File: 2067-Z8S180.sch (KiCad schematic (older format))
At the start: 13 parts, among them J1 Conn_02x12_Odd_Even, J2 Conn_02x30_Odd_Even, U1 Z8S18020FSG, U2 IS61WV10248EDBLL-10TLI

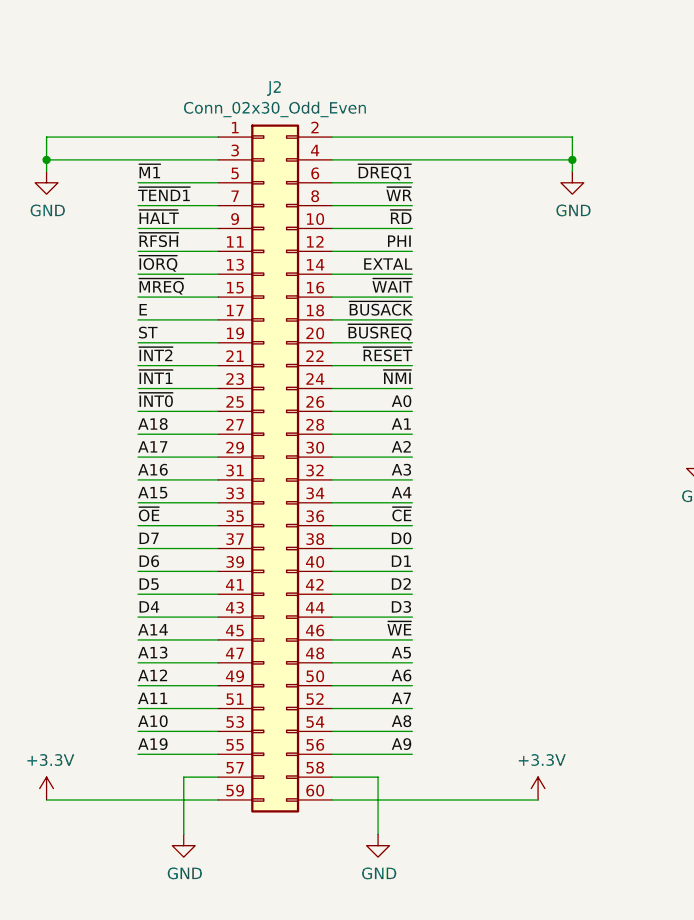
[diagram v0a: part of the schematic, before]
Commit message: Add FPGA pin number reference
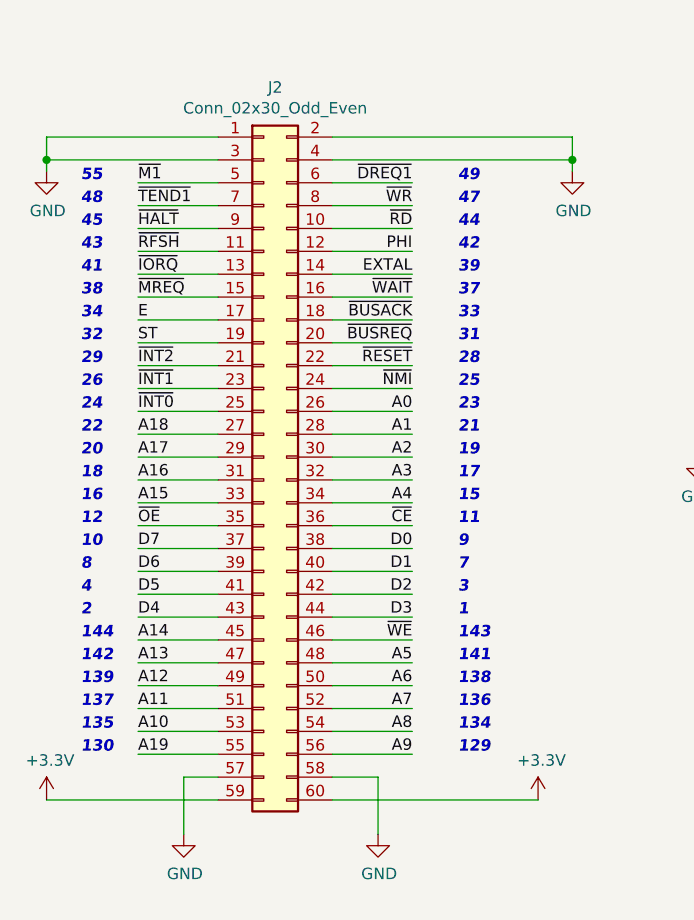
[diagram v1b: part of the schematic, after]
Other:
- note added: "1"
- note added: "10"
- note added: "11"
- note added: "12"
- note added: "129"
- note added: "130"
- note added: "134"
- note added: "135"
- note added: "136"
- note added: "137"
- note added: "138"
- note added: "139"
- note added: "141"
- note added: "142"
- note added: "143"
- note added: "144"
- note added: "15"
- note added: "16"
- note added: "17"
- note added: "18"
- note added: "19"
- note added: "2"
- note added: "20"
- note added: "21"
- note added: "22"
- note added: "23"
- note added: "24"
- note added: "25"
- note added: "26"
- note added: "28"
- note added: "29"
- note added: "3"
- note added: "31"
- note added: "32"
- note added: "33"
- note added: "34"
- note added: "37"
- note added: "38"
- note added: "39"
- note added: "4"
- note added: "41"
- note added: "42"
- note added: "43"
- note added: "44"
- note added: "45"
- note added: "47"
- note added: "48"
- note added: "49"
- note added: "55"
- note added: "7"
- note added: "8"
- note added: "9"
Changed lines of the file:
@@
 	1    0    0    -1
 $EndComp
+Text Notes 4500 3800 0    50   Italic 10
+55
+Text Notes 4500 3900 0    50   Italic 10
+48
+Text Notes 4500 4000 0    50   Italic 10
+45
+Text Notes 4500 4100 0    50   Italic 10
+43
+Text Notes 4500 4200 0    50   Italic 10
+41
+Text Notes 4500 4300 0    50   Italic 10
+38
+Text Notes 4500 4400 0    50   Italic 10
+34
+Text Notes 4500 4500 0    50   Italic 10
+32
+Text Notes 4500 4600 0    50   Italic 10
+29
+Text Notes 4500 4700 0    50   Italic 10
+26
+Text Notes 4500 4800 0    50   Italic 10
+24
+Text Notes 4500 4900 0    50   Italic 10
+22
+Text Notes 4500 5000 0    50   Italic 10
+20
+Text Notes 4500 5100 0    50   Italic 10
+18
+Text Notes 4500 5200 0    50   Italic 10
+16
+Text Notes 4500 5300 0    50   Italic 10
+12
+Text Notes 4500 5400 0    50   Italic 10
+10
+Text Notes 4500 5500 0    50   Italic 10
+8
+Text Notes 4500 5600 0    50   Italic 10
+4
+Text Notes 4500 5700 0    50   Italic 10
+2
+Text Notes 4500 5800 0    50   Italic 10
+144
+Text Notes 4500 5900 0    50   Italic 10
+142
+Text Notes 4500 6000 0    50   Italic 10
+139
+Text Notes 4500 6100 0    50   Italic 10
+137
+Text Notes 4500 6200 0    50   Italic 10
+135
+Text Notes 4500 6300 0    50   Italic 10
+130
+Text Notes 6150 6300 0    50   Italic 10
+129
+Text Notes 6150 6200 0    50   Italic 10
+134
+Text Notes 6150 6100 0    50   Italic 10
+136
+Text Notes 6150 6000 0    50   Italic 10
+138
+Text Notes 6150 5900 0    50   Italic 10
+141
+Text Notes 6150 5800 0    50   Italic 10
+143
+Text Notes 6150 5700 0    50   Italic 10
+1
+Text Notes 6150 5600 0    50   Italic 10
+3
+Text Notes 6150 5500 0    50   Italic 10
+7
+Text Notes 6150 5400 0    50   Italic 10
+9
+Text Notes 6150 5300 0    50   Italic 10
+11
+Text Notes 6150 5200 0    50   Italic 10
+15
+Text Notes 6150 5100 0    50   Italic 10
+17
+Text Notes 6150 5000 0    50   Italic 10
+19
+Text Notes 6150 4900 0    50   Italic 10
+21
+Text Notes 6150 4800 0    50   Italic 10
+23
+Text Notes 6150 4700 0    50   Italic 10
+25
+Text Notes 6150 4600 0    50   Italic 10
+28
+Text Notes 6150 4500 0    50   Italic 10
+31
+Text Notes 6150 4400 0    50   Italic 10
+33
+Text Notes 6150 4300 0    50   Italic 10
+37
+Text Notes 6150 4200 0    50   Italic 10
+39
+Text Notes 6150 4100 0    50   Italic 10
+42
+Text Notes 6150 4000 0    50   Italic 10
+44
+Text Notes 6150 3900 0    50   Italic 10
+47
+Text Notes 6150 3800 0    50   Italic 10
+49
 $EndSCHEMATC

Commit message: Thermal relief, SRAM A20
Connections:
- net GND: now also U2.42 (A20)
- no-connect marks 8 -> 7
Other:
- note added: "Copyright (C) 2019, 2023 John Winans\n\nThis documentation describes Open Hardware and is licensed under the CERN OHL v. 1.2.\n\nYou may redistribute and modify this documentation under the terms of the CERN OHL v.1.2. (http://ohwr.org/cernohl). \nThis documentation is distributed WITHOUT ANY EXPRESS OR IMPLIED WARRANTY, INCLUDING OF MERCHANTABILITY, \nSATISFACTORY QUALITY AND FITNESS FOR A PARTI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"
- note added: "IS61WV5128FBLL-10TLI\nIS61WV10248EDBLL-10TLI\nIS61WV20488BLL-10TLI"
- note added: "Viable SRAM substitutes:"
- note added: "https://github.com/johnwinans/2067-Z8S180"
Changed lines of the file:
@@
 Sheet 1 1
 Title "Z8S180 Breakout"
-Date "2023-12-10"
-Rev "1.1"
+Date "2024-02-19"
+Rev "1.2"
 Comp ""
 Comment1 ""
@@
 Text Label 12500 5900 0    50   ~ 0
 A19
-NoConn ~ 12950 6000
 Text Label 12500 6150 0    50   ~ 0
 ~CE
@@
 Text Notes 6150 3800 0    50   Italic 10
 49
+$Comp
+L power:GND #PWR?
+U 1 1 65D61870
+P 12100 6000
+F 0 "#PWR?" H 12100 5750 50  0001 C CNN
+F 1 "GND" H 12105 5827 50  0000 C CNN
+F 2 "" H 12100 6000 50  0001 C CNN
+F 3 "" H 12100 6000 50  0001 C CNN
+	1    12100 6000
+	1    0    0    -1
+$EndComp
+Wire Wire Line
+	12950 6000 12100 6000
+Text Notes 14350 5600 0    51   ~ 0
+IS61WV5128FBLL-10TLI\nIS61WV10248EDBLL-10TLI\nIS61WV20488BLL-10TLI
+Text Notes 14350 5300 0    50   ~ 10
+Viable SRAM substitutes:
+Text Notes 12300 9850 0    39   ~ 0
+Copyright (C) 2019, 2023 John Winans\n\nThis documentation describes Open Hardware and is licensed under the CERN OHL v. 1.2.\n\nYou may redistribute and modify this documentation under the terms of the CERN OHL v.1.2. (http://ohwr.org/cernohl). \nThis documentation is distributed WITHOUT ANY EXPRESS OR IMPLIED WARRANTY, INCLUDING OF MERCHANTABILITY, \nSATISFACTORY QUALITY AND FITNESS FOR A PARTICULAR PURPOSE.  Please see the CERN OHL v.1.2 for applicable conditions\n\nIf you chose to manufacture products based on this design, please notify me (see license section 4.2) via john@winans.org\n
+Text Notes 14700 9250 0    50   ~ 10
+https://github.com/johnwinans/2067-Z8S180
 $EndSCHEMATC
